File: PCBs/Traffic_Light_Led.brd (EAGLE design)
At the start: 37 x 27.5 mm, 10 parts

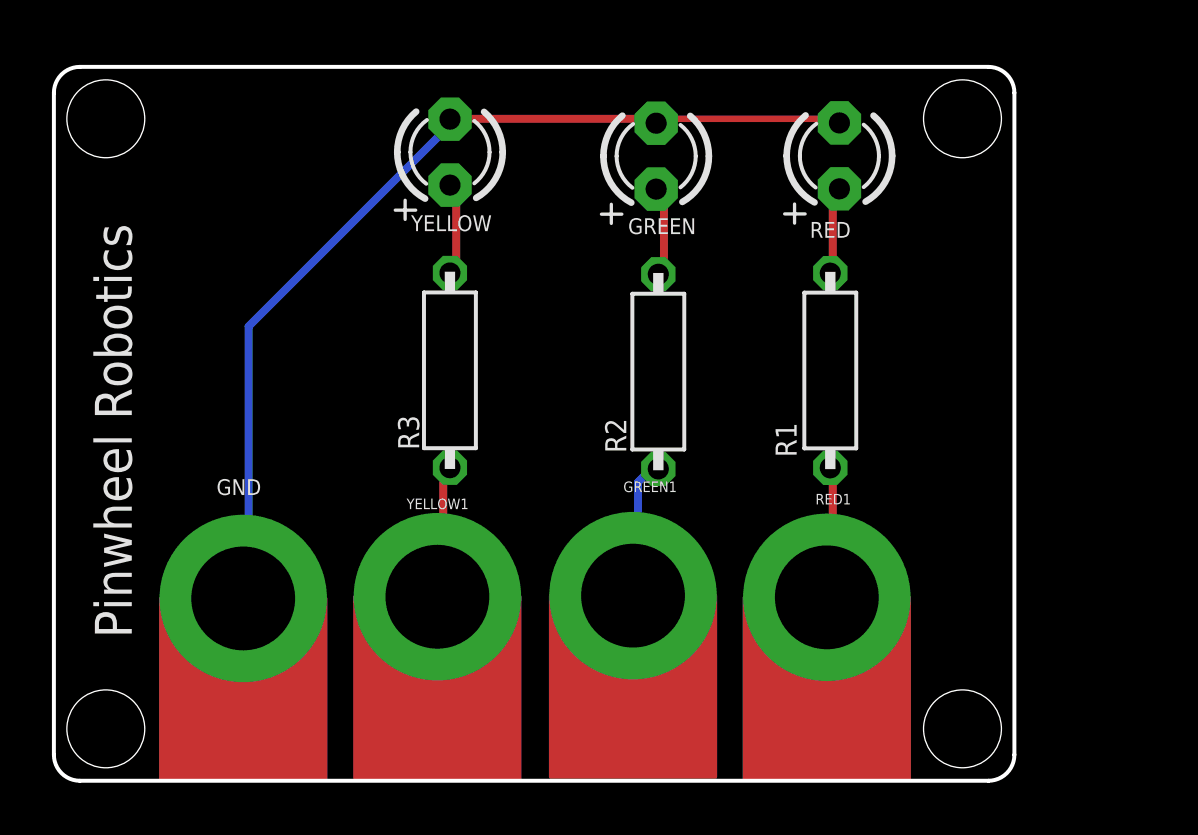
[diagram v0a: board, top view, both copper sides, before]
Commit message: Update for Dim width is 42 length is 28 for type 2 pcb
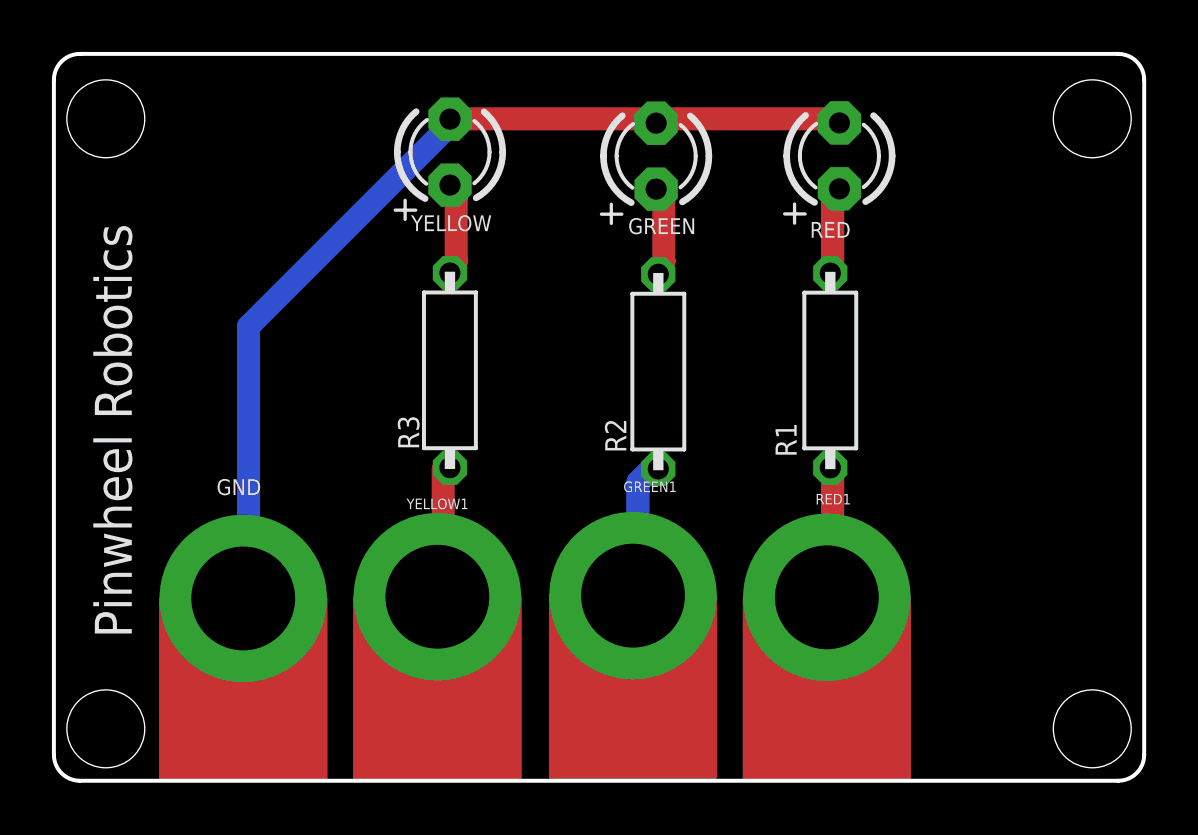
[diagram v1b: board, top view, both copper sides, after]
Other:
- board size 37 x 27.5 mm -> 42 x 28 mm
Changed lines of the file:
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@@
 <drawing>
 <settings>
-<setting alwaysvectorfont="no"/>
+<setting alwaysvectorfont="yes"/>
 <setting verticaltext="up"/>
 </settings>
@@
 <plain>
 <hole x="2" y="2" drill="3"/>
-<hole x="35" y="2" drill="3"/>
-<hole x="35" y="25.5" drill="3"/>
+<hole x="40" y="2" drill="3"/>
+<hole x="40" y="25.5" drill="3"/>
 <hole x="2" y="25.5" drill="3"/>
 <text x="3" y="5.5" size="1.4224" layer="21" rot="R90">Pinwheel Robotics</text>
 <text x="34.5" y="6.5" size="1.4224" layer="22" rot="MR90">care@pinwheel.in</text>
-<wire x1="0" y1="26.5" x2="0" y2="1" width="0.1524" layer="20"/>
+<wire x1="0" y1="27" x2="0" y2="1" width="0.1524" layer="20"/>
 <wire x1="0" y1="1" x2="1" y2="0" width="0.1524" layer="20" curve="90"/>
-<wire x1="1" y1="0" x2="36" y2="0" width="0.1524" layer="20"/>
-<wire x1="36" y1="0" x2="37" y2="1" width="0.1524" layer="20" curve="90"/>
-<wire x1="37" y1="1" x2="37" y2="26.5" width="0.1524" layer="20"/>
-<wire x1="37" y1="26.5" x2="36" y2="27.5" width="0.1524" layer="20" curve="90"/>
-<wire x1="36" y1="27.5" x2="1" y2="27.5" width="0.1524" layer="20"/>
-<wire x1="1" y1="27.5" x2="0" y2="26.5" width="0.1524" layer="20" curve="90"/>
-<dimension x1="-0.5" y1="27.5" x2="-0.5" y2="0" x3="-2.5" y3="13.75" textsize="1.778" layer="1"/>
-<dimension x1="0" y1="28" x2="37" y2="28" x3="18.5" y3="29" textsize="1.778" layer="1"/>
+<wire x1="1" y1="0" x2="41" y2="0" width="0.1524" layer="20"/>
+<wire x1="41" y1="0" x2="42" y2="1" width="0.1524" layer="20" curve="90"/>
+<wire x1="42" y1="1" x2="42" y2="27" width="0.1524" layer="20"/>
+<wire x1="42" y1="27" x2="41" y2="28" width="0.1524" layer="20" curve="90"/>
+<wire x1="41" y1="28" x2="1" y2="28" width="0.1524" layer="20"/>
+<wire x1="1" y1="28" x2="0" y2="27" width="0.1524" layer="20" curve="90"/>
 </plain>
 <attributes>
@@
 <param name="mdDrill" value="6mil"/>
 <param name="mdSmdStop" value="0mil"/>
-<param name="msWidth" value="10mil"/>
+<param name="msWidth" value="35mil"/>
 <param name="msDrill" value="0.35mm"/>
 <param name="msMicroVia" value="9.99mm"/>
@@
 <contactref element="RED1" pad="PAD"/>
 <contactref element="R1" pad="1"/>
-<wire x1="30" y1="7.5" x2="30" y2="12" width="0.3048" layer="1"/>
-<wire x1="30" y1="12" x2="29.908" y2="12.054" width="0.254" layer="1"/>
-<wire x1="30" y1="7.5" x2="29.775" y2="7.066" width="0.254" layer="1"/>
+<wire x1="30" y1="7.5" x2="30" y2="12" width="0.889" layer="1"/>
+<wire x1="30" y1="12" x2="29.908" y2="12.054" width="0.889" layer="1"/>
+<wire x1="30" y1="7.5" x2="29.775" y2="7.066" width="0.889" layer="1"/>
 </signal>
 <signal name="N$3">
 <contactref element="GREEN" pad="A"/>
 <contactref element="R2" pad="2"/>
-<wire x1="23.5" y1="22.5" x2="23.5" y2="20" width="0.3048" layer="1"/>
-<wire x1="23.5" y1="20" x2="23.283" y2="19.511" width="0.3048" layer="1"/>
-<wire x1="23.5" y1="22.5" x2="23.2" y2="22.791" width="0.254" layer="1"/>
+<wire x1="23.5" y1="22.5" x2="23.5" y2="20" width="0.889" layer="1"/>
+<wire x1="23.5" y1="20" x2="23.283" y2="19.511" width="0.889" layer="1"/>
+<wire x1="23.5" y1="22.5" x2="23.2" y2="22.791" width="0.889" layer="1"/>
 </signal>
 <signal name="N$5">
 <contactref element="YELLOW" pad="A"/>
 <contactref element="R3" pad="2"/>
-<wire x1="15.5" y1="22.5" x2="15.5" y2="20" width="0.3048" layer="1"/>
-<wire x1="15.5" y1="20" x2="15.256" y2="19.56" width="0.254" layer="1"/>
-<wire x1="15.5" y1="22.5" x2="15.258" y2="22.946" width="0.254" layer="1"/>
+<wire x1="15.5" y1="22.5" x2="15.5" y2="20" width="0.889" layer="1"/>
+<wire x1="15.5" y1="20" x2="15.256" y2="19.56" width="0.889" layer="1"/>
+<wire x1="15.5" y1="22.5" x2="15.258" y2="22.946" width="0.889" layer="1"/>
 </signal>
 <signal name="GND">
@@
 <contactref element="YELLOW" pad="K"/>
 <contactref element="GND" pad="PAD"/>
-<wire x1="30" y1="25.5" x2="23.5" y2="25.5" width="0.254" layer="1"/>
-<wire x1="23.5" y1="25.5" x2="23.2" y2="25.331" width="0.254" layer="1"/>
-<wire x1="30" y1="25.5" x2="30.259" y2="25.341" width="0.254" layer="1"/>
-<wire x1="23" y1="25.5" x2="15.5" y2="25.5" width="0.3048" layer="1"/>
-<wire x1="15.5" y1="25.5" x2="15.258" y2="25.486" width="0.254" layer="1"/>
-<wire x1="23" y1="25.5" x2="23.2" y2="25.331" width="0.254" layer="1"/>
-<wire x1="7.5" y1="17.5" x2="15" y2="25" width="0.3048" layer="16"/>
-<wire x1="7.5" y1="7.5" x2="7.5" y2="17.5" width="0.3048" layer="16"/>
-<wire x1="15" y1="25" x2="15.258" y2="25.486" width="0.254" layer="16"/>
-<wire x1="7.5" y1="7.5" x2="7.293" y2="7.023" width="0.254" layer="16"/>
+<wire x1="30" y1="25.5" x2="23.5" y2="25.5" width="0.889" layer="1"/>
+<wire x1="23.5" y1="25.5" x2="23.2" y2="25.331" width="0.889" layer="1"/>
+<wire x1="30" y1="25.5" x2="30.259" y2="25.341" width="0.889" layer="1"/>
+<wire x1="23" y1="25.5" x2="15.5" y2="25.5" width="0.889" layer="1"/>
+<wire x1="15.5" y1="25.5" x2="15.258" y2="25.486" width="0.889" layer="1"/>
+<wire x1="23" y1="25.5" x2="23.2" y2="25.331" width="0.889" layer="1"/>
+<wire x1="7.5" y1="17.5" x2="15" y2="25" width="0.889" layer="16"/>
+<wire x1="7.5" y1="7.5" x2="7.5" y2="17.5" width="0.889" layer="16"/>
+<wire x1="15" y1="25" x2="15.258" y2="25.486" width="0.889" layer="16"/>
+<wire x1="7.5" y1="7.5" x2="7.293" y2="7.023" width="0.889" layer="16"/>
 </signal>
 <signal name="N$2">
 <contactref element="YELLOW1" pad="PAD"/>
 <contactref element="R3" pad="1"/>
-<wire x1="15" y1="7.5" x2="15" y2="12" width="0.3048" layer="1"/>
-<wire x1="15" y1="12" x2="15.256" y2="12.06" width="0.254" layer="1"/>
-<wire x1="15" y1="7.5" x2="14.773" y2="7.089" width="0.3048" layer="1"/>
+<wire x1="15" y1="7.5" x2="15" y2="12" width="0.889" layer="1"/>
+<wire x1="15" y1="12" x2="15.256" y2="12.06" width="0.889" layer="1"/>
+<wire x1="15" y1="7.5" x2="14.773" y2="7.089" width="0.889" layer="1"/>
 </signal>
 <signal name="N$4">
 <contactref element="GREEN1" pad="PAD"/>
 <contactref element="R2" pad="1"/>
-<wire x1="22.5" y1="11.5" x2="23" y2="12" width="0.3048" layer="16"/>
-<wire x1="22.5" y1="7.5" x2="22.5" y2="11.5" width="0.3048" layer="16"/>
-<wire x1="23" y1="12" x2="23.283" y2="12.011" width="0.254" layer="16"/>
-<wire x1="22.5" y1="7.5" x2="22.309" y2="7.131" width="0.3048" layer="16"/>
+<wire x1="22.5" y1="11.5" x2="23" y2="12" width="0.889" layer="16"/>
+<wire x1="22.5" y1="7.5" x2="22.5" y2="11.5" width="0.889" layer="16"/>
+<wire x1="23" y1="12" x2="23.283" y2="12.011" width="0.889" layer="16"/>
+<wire x1="22.5" y1="7.5" x2="22.309" y2="7.131" width="0.889" layer="16"/>
 </signal>
 <signal name="N$6">
 <contactref element="RED" pad="A"/>
 <contactref element="R1" pad="2"/>
-<wire x1="30" y1="22.5" x2="30" y2="20" width="0.3048" layer="1"/>
-<wire x1="30" y1="20" x2="29.908" y2="19.554" width="0.254" layer="1"/>
-<wire x1="30" y1="22.5" x2="30.259" y2="22.801" width="0.254" layer="1"/>
+<wire x1="30" y1="22.5" x2="30" y2="20" width="0.889" layer="1"/>
+<wire x1="30" y1="20" x2="29.908" y2="19.554" width="0.889" layer="1"/>
+<wire x1="30" y1="22.5" x2="30.259" y2="22.801" width="0.889" layer="1"/>
 </signal>
 </signals>

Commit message: Corrected hole position for some design , made transistor as switch as category 1
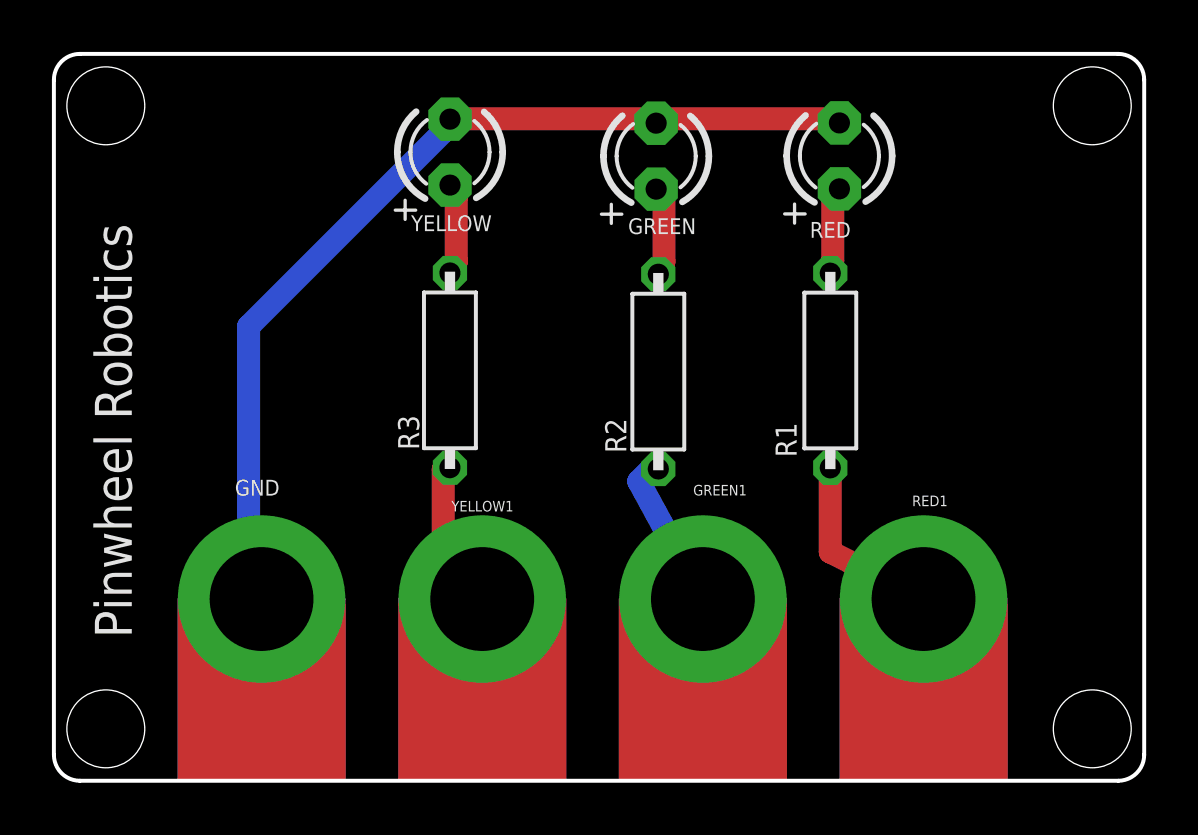
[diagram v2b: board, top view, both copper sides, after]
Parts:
- moved RED1 3.73 mm to (33.5, 7.00)
- moved GREEN1 2.69 mm to (25.0, 7.00)
- moved YELLOW1 1.73 mm to (16.5, 7.00)
- moved GND 0.71 mm to (8.00, 7.00)
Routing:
- net N$1: track 5.10 -> 7.27 mm
- net N$4: track 5.41 -> 6.11 mm
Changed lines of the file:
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@@
 <drawing>
 <settings>
-<setting alwaysvectorfont="yes"/>
+<setting alwaysvectorfont="no"/>
 <setting verticaltext="up"/>
 </settings>
@@
 <hole x="2" y="2" drill="3"/>
 <hole x="40" y="2" drill="3"/>
-<hole x="40" y="25.5" drill="3"/>
-<hole x="2" y="25.5" drill="3"/>
+<hole x="40" y="26" drill="3"/>
+<hole x="2" y="26" drill="3"/>
 <text x="3" y="5.5" size="1.4224" layer="21" rot="R90">Pinwheel Robotics</text>
 <text x="34.5" y="6.5" size="1.4224" layer="22" rot="MR90">care@pinwheel.in</text>
@@
 <attribute name="VALUE" x="24.851" y="25.966" size="1.27" layer="27" ratio="10" rot="R90"/>
 </element>
-<element name="GREEN1" library="microbit" package="MICROBIT_PAD" value="MICROBIT_PAD" x="22.309" y="7.131" smashed="yes">
-<attribute name="NAME" x="21.935" y="11.121" size="0.4064" layer="21" font="vector"/>
+<element name="GREEN1" library="microbit" package="MICROBIT_PAD" value="MICROBIT_PAD" x="25" y="7" smashed="yes">
+<attribute name="NAME" x="24.626" y="10.99" size="0.4064" layer="21" font="vector"/>
 </element>
 <element name="R1" library="we-rcl" package="R0207/7" value="330" x="29.908" y="15.804" smashed="yes" rot="R90">
@@
 <attribute name="VALUE" x="31.91" y="25.976" size="1.27" layer="27" ratio="10" rot="R90"/>
 </element>
-<element name="RED1" library="microbit" package="MICROBIT_PAD" value="MICROBIT_PAD" x="29.775" y="7.066" smashed="yes">
-<attribute name="NAME" x="29.335" y="10.644" size="0.4064" layer="21" font="vector"/>
-</element>
-<element name="GND" library="microbit" package="MICROBIT_PAD" value="MICROBIT_PAD" x="7.293" y="7.023" smashed="yes">
-<attribute name="NAME" x="6.263" y="11.007" size="0.6096" layer="21" font="vector"/>
+<element name="RED1" library="microbit" package="MICROBIT_PAD" value="MICROBIT_PAD" x="33.5" y="7" smashed="yes">
+<attribute name="NAME" x="33.06" y="10.578" size="0.4064" layer="21" font="vector"/>
+</element>
+<element name="GND" library="microbit" package="MICROBIT_PAD" value="MICROBIT_PAD" x="8" y="7" smashed="yes">
+<attribute name="NAME" x="6.97" y="10.984" size="0.6096" layer="21" font="vector"/>
 </element>
 <element name="YELLOW" library="adafruit" library_urn="urn:adsk.eagle:library:420" package="LED3MM" package3d_urn="urn:adsk.eagle:package:6240537/1" value="" x="15.258" y="24.216" smashed="yes" rot="R90">
@@
 <attribute name="VALUE" x="16.909" y="26.121" size="1.27" layer="27" ratio="10" rot="R90"/>
 </element>
-<element name="YELLOW1" library="microbit" package="MICROBIT_PAD" value="MICROBIT_PAD" x="14.773" y="7.089" smashed="yes">
-<attribute name="NAME" x="13.585" y="10.463" size="0.4064" layer="21" font="vector"/>
+<element name="YELLOW1" library="microbit" package="MICROBIT_PAD" value="MICROBIT_PAD" x="16.5" y="7" smashed="yes">
+<attribute name="NAME" x="15.312" y="10.374" size="0.4064" layer="21" font="vector"/>
 </element>
 </elements>
@@
 <contactref element="RED1" pad="PAD"/>
 <contactref element="R1" pad="1"/>
-<wire x1="30" y1="7.5" x2="30" y2="12" width="0.889" layer="1"/>
-<wire x1="30" y1="12" x2="29.908" y2="12.054" width="0.889" layer="1"/>
-<wire x1="30" y1="7.5" x2="29.775" y2="7.066" width="0.889" layer="1"/>
+<wire x1="33.5" y1="7" x2="29.908" y2="8.811565625" width="0.889" layer="1"/>
+<wire x1="29.908" y1="12.054" x2="29.908" y2="8.811565625" width="0.889" layer="1"/>
 </signal>
 <signal name="N$3">
@@
 <wire x1="23" y1="25.5" x2="23.2" y2="25.331" width="0.889" layer="1"/>
 <wire x1="7.5" y1="17.5" x2="15" y2="25" width="0.889" layer="16"/>
-<wire x1="7.5" y1="7.5" x2="7.5" y2="17.5" width="0.889" layer="16"/>
+<wire x1="7.5" y1="8.85035" x2="7.5" y2="17.5" width="0.889" layer="16"/>
 <wire x1="15" y1="25" x2="15.258" y2="25.486" width="0.889" layer="16"/>
-<wire x1="7.5" y1="7.5" x2="7.293" y2="7.023" width="0.889" layer="16"/>
+<wire x1="7.5" y1="8.85035" x2="8" y2="7" width="0.889" layer="16"/>
 </signal>
 <signal name="N$2">
 <contactref element="YELLOW1" pad="PAD"/>
 <contactref element="R3" pad="1"/>
-<wire x1="15" y1="7.5" x2="15" y2="12" width="0.889" layer="1"/>
+<wire x1="15" y1="9.393859375" x2="15" y2="12" width="0.889" layer="1"/>
 <wire x1="15" y1="12" x2="15.256" y2="12.06" width="0.889" layer="1"/>
-<wire x1="15" y1="7.5" x2="14.773" y2="7.089" width="0.889" layer="1"/>
+<wire x1="15" y1="9.393859375" x2="16.5" y2="7" width="0.889" layer="1"/>
 </signal>
 <signal name="N$4">
 <contactref element="GREEN1" pad="PAD"/>
 <contactref element="R2" pad="1"/>
-<wire x1="22.5" y1="11.5" x2="23" y2="12" width="0.889" layer="16"/>
-<wire x1="22.5" y1="7.5" x2="22.5" y2="11.5" width="0.889" layer="16"/>
+<wire x1="22.531325" y1="11.531325" x2="23" y2="12" width="0.889" layer="16"/>
 <wire x1="23" y1="12" x2="23.283" y2="12.011" width="0.889" layer="16"/>
-<wire x1="22.5" y1="7.5" x2="22.309" y2="7.131" width="0.889" layer="16"/>
+<wire x1="22.531325" y1="11.531325" x2="25" y2="7" width="0.889" layer="16"/>
 </signal>
 <signal name="N$6">
